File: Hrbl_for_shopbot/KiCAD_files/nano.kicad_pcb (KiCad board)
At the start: 2 copper layers, 79.8 x 140.1 mm, 69 parts, among them P1 Digital, P2 Analog, P3 CONN_01X01, P4 CONN_01X01, P5 CONN_01X01, P6 CONN_01X01, U1 SFH6206-3T, U10 SFH6206-3T, U11 SFH6206-3T, U12 SFH6206-3T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

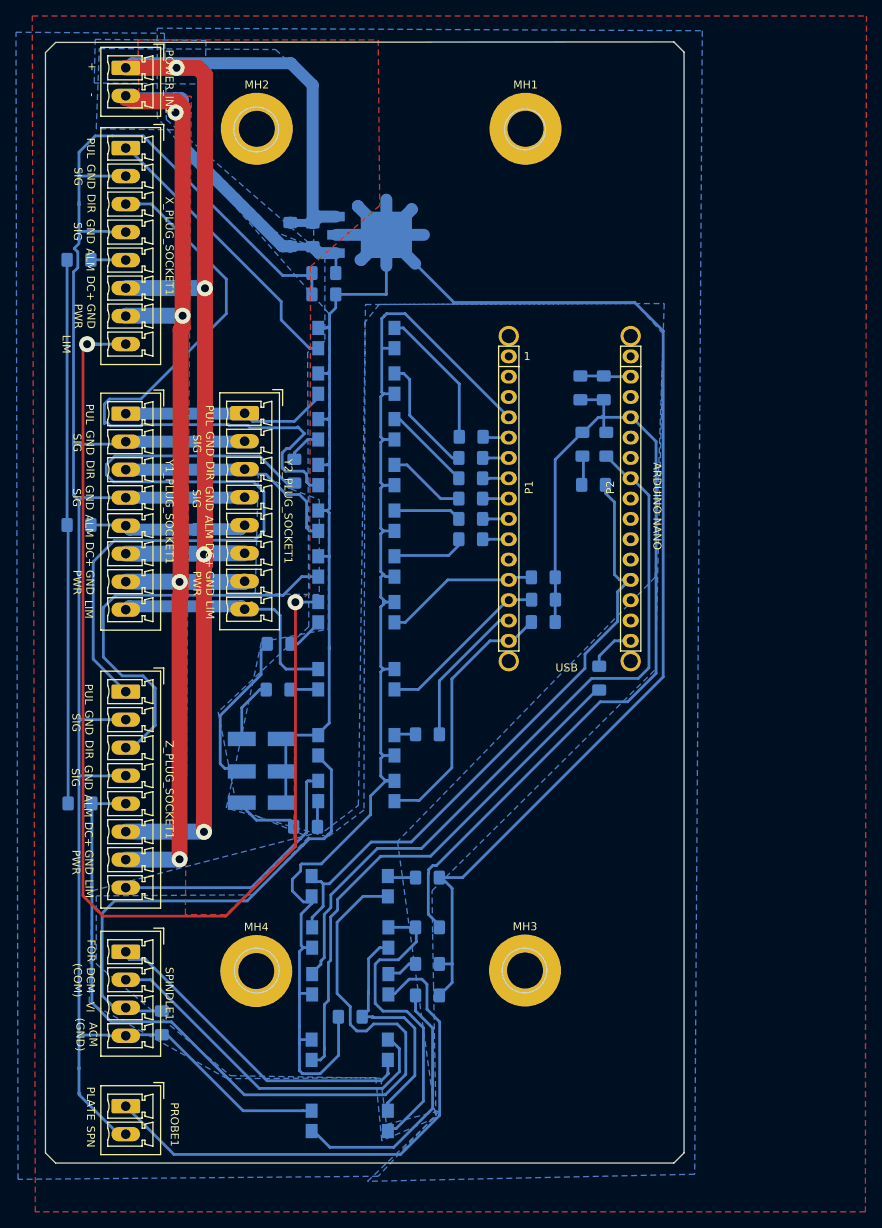
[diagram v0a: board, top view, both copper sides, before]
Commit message: Updated with 24V Contactor signal and PWM filter
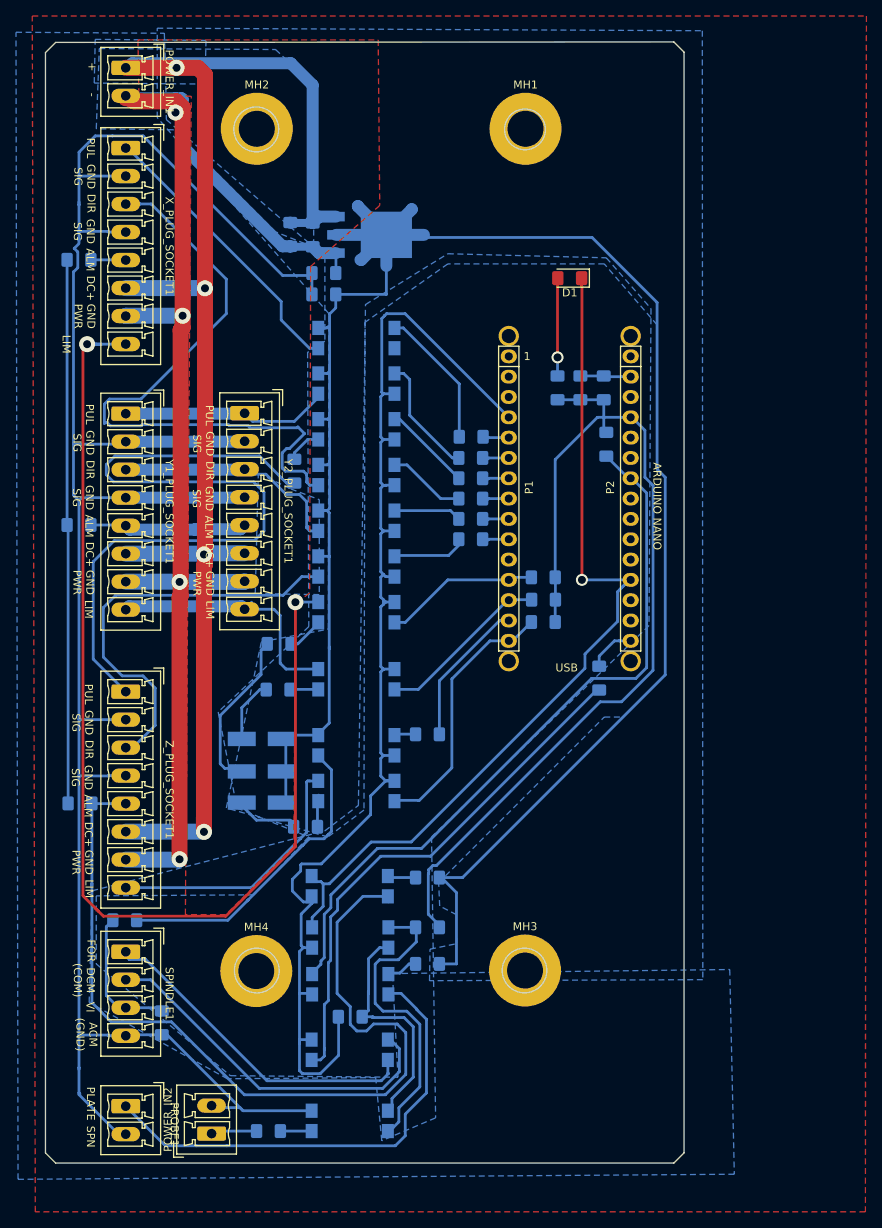
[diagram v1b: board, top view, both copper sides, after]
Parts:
- added POWER_IN2: Conn_01x02, Connector_Phoenix_MC:PhoenixContact_MCV_1,5_2-G-3.5_1x02_P3.50mm_Vertical, F.Cu at (102.3, 168.4)
- added R27: R 1k, Resistor_SMD:R_1206_3216Metric_Pad1.42x1.75mm_HandSolder, B.Cu at (91.4, 141.7)
- C4: value 100nF (0.1uF) -> 10uF
- D1: moved to F.Cu
- R12: value 220 -> R 1k
- moved R12 26.1 mm to (109.4, 168.1), turned to 180 degrees
- moved D1 26.0 mm to (147.1, 61.5)
- moved R21 7.70 mm to (145.5, 75.2), turned to 270 degrees
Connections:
- C4 pad 1: /VI -> Net-(C4-Pad1)
- R12 pad 2: 5V_ISO -> 24V_CONTACTOR_SIGNAL
- SPINDLE1 pad 3: /VI -> Net-(C4-Pad1)
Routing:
- net ABORT: track 81.4 -> 111.4 mm, vias 0 -> 1
- net Net-(R12-Pad1): track 33.2 -> 3.91 mm
- net /VI: track 61.1 -> 39.3 mm
- net Net-(C4-Pad1): track 0.00 -> 18.9 mm
- net 5V_ISO: track 260.2 -> 249.1 mm
- net Net-(D1-Pad2): track 3.53 -> 12.2 mm, vias 0 -> 1
- net /PROBE_PLATE: track 66.6 -> 59.3 mm
- net 24V_CONTACTOR_SIGNAL: track 0.00 -> 5.92 mm
- net GNDS: track 267.8 -> 271.8 mm
- net +5V: track 119.4 -> 121.8 mm
- net GND: track 193.7 -> 191.5 mm
- net Net-(R15-Pad1): track 39.3 -> 38.7 mm
